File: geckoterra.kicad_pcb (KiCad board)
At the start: 2 copper layers, 50 x 50 mm, 24 parts, among them J1 AC_Output, J6 Conn_01x02, J7 Conn_01x02, J8 Conn_01x02, K1 SANYOU_SRD_Form_C, P1 AC_Input, Q1 2N3904, Q2 Q_NMOS_GDS, U1 PC817, U2 4N25

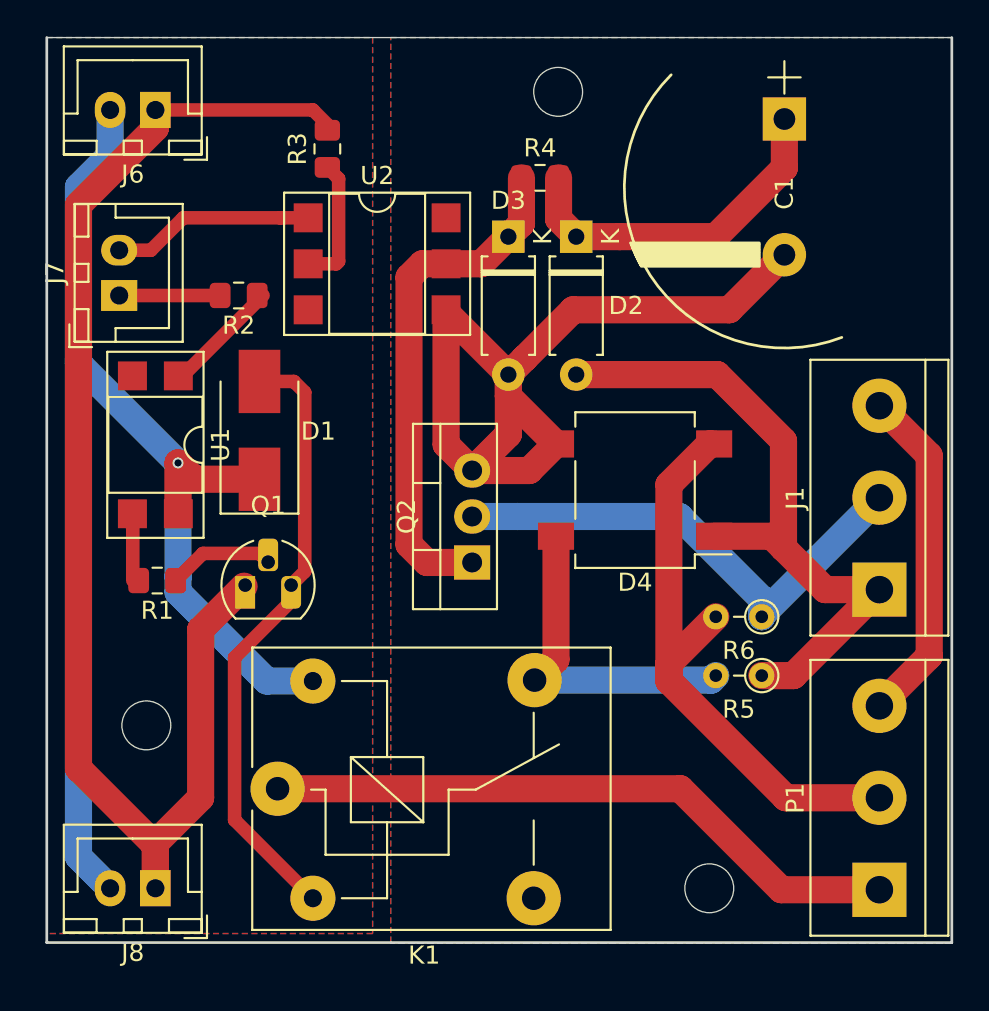
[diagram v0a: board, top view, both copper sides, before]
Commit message: Repair PCB considering footprints
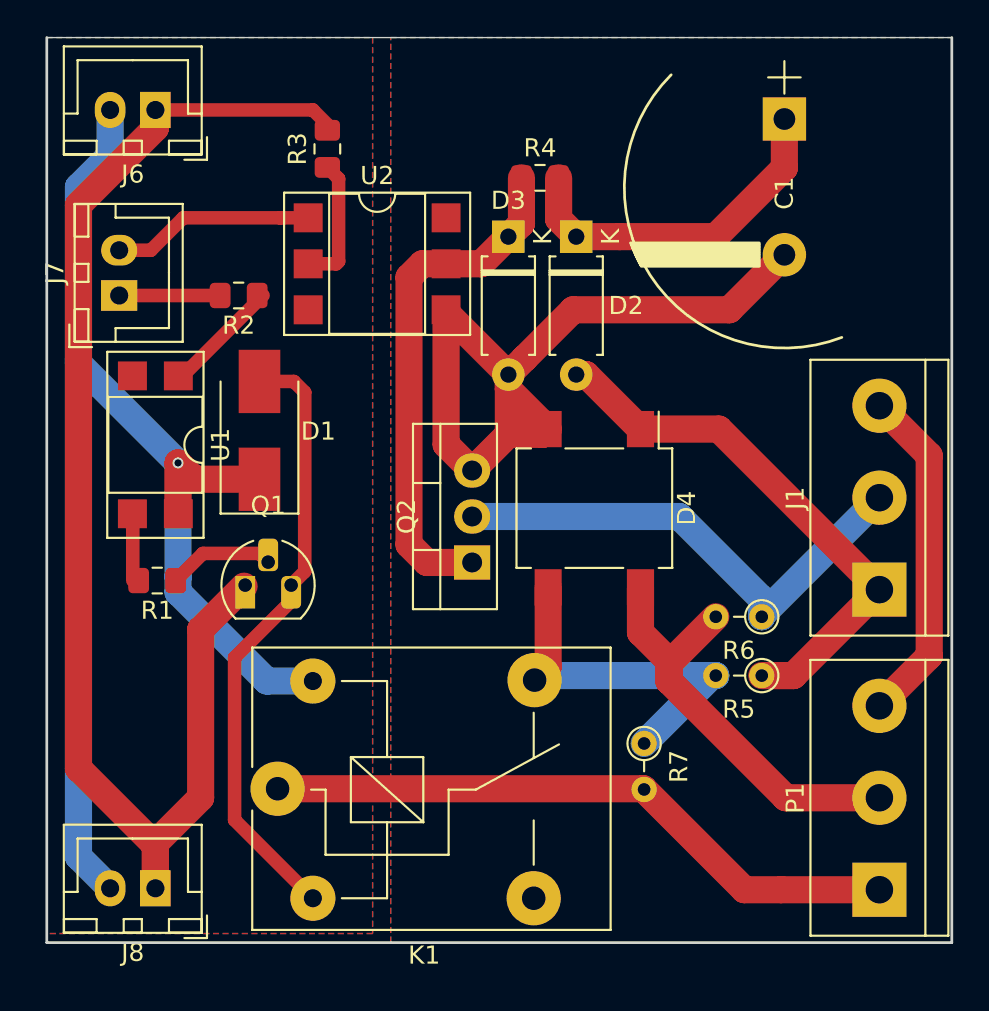
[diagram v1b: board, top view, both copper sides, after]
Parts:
- removed SC1 (x2), SC2: MountingHole_2.7mm_M2.5, Mounting_Holes:MountingHole_2.7mm_M2.5
- added R7: Shunt, Resistor_THT:R_Axial_DIN0204_L3.6mm_D1.6mm_P2.54mm_Vertical, F.Cu at (83.0, 89.0)
- moved D4 2.46 mm to (80.2, 76.0), turned to 270 degrees
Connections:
- D4 pad 2: Net-(D4-Pad2) -> Net-(C1-Pad2)
- D4 pad 3: Net-(C1-Pad2) -> Net-(D4-Pad3)
- K1 pad 4: Net-(D4-Pad4) -> Net-(D4-Pad3)
- P1 pad 2: Net-(D4-Pad2) -> Net-(D4-Pad4)
- R5 pad 2: Net-(D4-Pad4) -> Net-(D4-Pad3)
- R6 pad 2: Net-(D4-Pad2) -> Net-(D4-Pad4)
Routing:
- net Net-(D4-Pad2): track 33.2 -> 0.00 mm
- net Net-(D4-Pad3): track 0.00 -> 21.1 mm
- net Net-(D2-Pad2): track 39.3 -> 31.7 mm
- net Net-(D4-Pad4): track 18.5 -> 24.7 mm
- net Net-(C1-Pad2): track 48.8 -> 44.8 mm

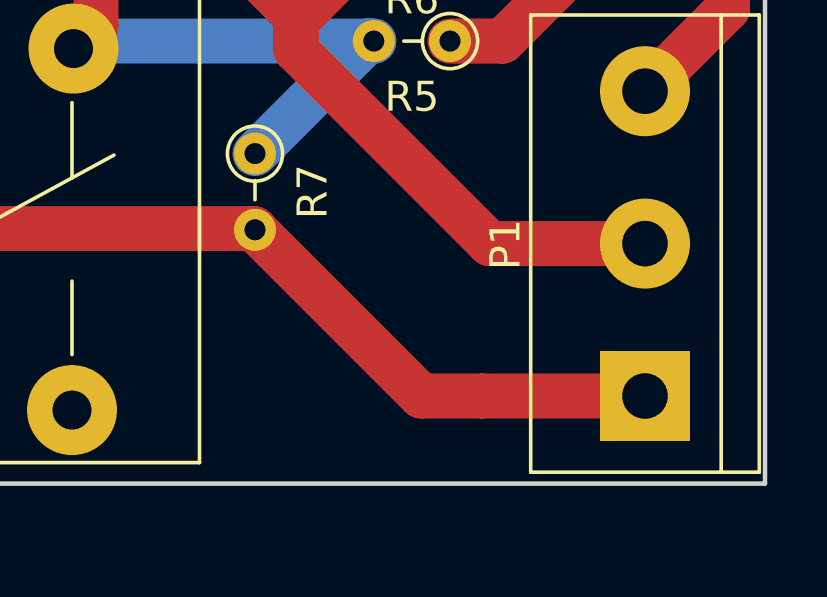
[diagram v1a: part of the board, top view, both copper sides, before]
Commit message: Add fuse
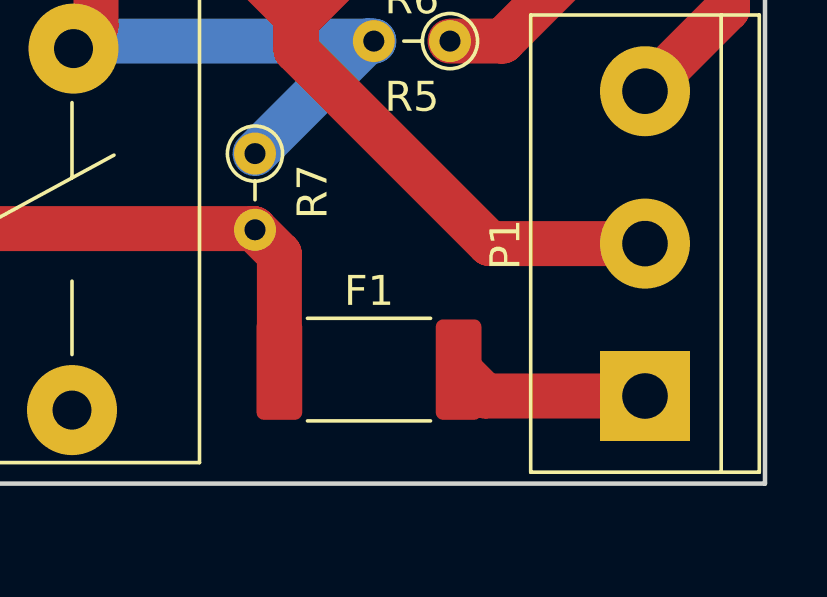
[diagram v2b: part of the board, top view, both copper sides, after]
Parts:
- added F1: Fuse, Fuse:Fuse_2512_6332Metric_Pad1.52x3.35mm_HandSolder, F.Cu at (86.8, 96.2)
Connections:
- K1 pad 1: Net-(K1-Pad1) -> Net-(F1-Pad1)
- P1 pad 1: Net-(K1-Pad1) -> Net-(F1-Pad2)
- R7 pad 2: Net-(K1-Pad1) -> Net-(F1-Pad1)
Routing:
- net Net-(K1-Pad1): track 35.6 -> 0.00 mm
- net Net-(F1-Pad1): track 0.00 -> 25.3 mm
- net Net-(F1-Pad2): track 0.00 -> 6.58 mm
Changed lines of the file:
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@@
     (thickness 1.6)
     (drawings 8)
-    (tracks 118)
+    (tracks 119)
     (zones 0)
-    (modules 22)
-    (nets 22)
+    (modules 23)
+    (nets 23)
   )
   (page A4)
@@
   (net 15 "Net-(R2-Pad1)")
   (net 16 "Net-(R3-Pad1)")
-  (net 17 "Net-(K1-Pad1)")
-  (net 18 "Net-(U2-Pad3)")
-  (net 19 "Net-(U2-Pad6)")
-  (net 20 "Net-(K1-Pad3)")
-  (net 21 "Net-(D4-Pad3)")
+  (net 17 "Net-(U2-Pad3)")
+  (net 18 "Net-(U2-Pad6)")
+  (net 19 "Net-(K1-Pad3)")
+  (net 20 "Net-(D4-Pad3)")
+  (net 21 "Net-(F1-Pad2)")
+  (net 22 "Net-(F1-Pad1)")
   (net_class Default "Ceci est la Netclass par défaut"
     (clearance 0.5)
@@
     (uvia_drill 0.1)
     (add_net "Net-(D4-Pad3)")
-    (add_net "Net-(K1-Pad1)")
+    (add_net "Net-(F1-Pad1)")
+    (add_net "Net-(F1-Pad2)")
     (add_net "Net-(K1-Pad3)")
     (add_net "Net-(U2-Pad3)")
@@
     (add_net "Net-(R3-Pad1)")
   )
+  (module Fuse:Fuse_2512_6332Metric_Pad1.52x3.35mm_HandSolder (layer F.Cu)
+    (at 86.8 96.2)
+    (descr "Fuse SMD 2512 (6332 Metric), square (rectangular) end terminal, IPC_7351 nominal with elongated pad for handsoldering. (Body size source: http://www.tortai-tech.com/upload/download/2011102023233369053.pdf), generated with kicad-footprint-generator")
+    (tags "resistor handsolder")
+    (attr smd)
+    (fp_text reference F1 (at 0 -2.62) (layer F.SilkS)
+      (effects (font (size 1 1) (thickness 0.15)))
+    )
+    (fp_text value Fuse (at 0 2.62) (layer F.Fab)
+      (effects (font (size 1 1) (thickness 0.15)))
+    )
+    (fp_line (start -3.15 1.6) (end -3.15 -1.6) (layer F.Fab) (width 0.1))
+    (fp_line (start -3.15 -1.6) (end 3.15 -1.6) (layer F.Fab) (width 0.1))
+    (fp_line (start 3.15 -1.6) (end 3.15 1.6) (layer F.Fab) (width 0.1))
+    (fp_line (start 3.15 1.6) (end -3.15 1.6) (layer F.Fab) (width 0.1))
+    (fp_line (start -2.052064 -1.71) (end 2.052064 -1.71) (layer F.SilkS) (width 0.12))
+    (fp_line (start -2.052064 1.71) (end 2.052064 1.71) (layer F.SilkS) (width 0.12))
+    (fp_line (start -4 1.92) (end -4 -1.92) (layer F.CrtYd) (width 0.05))
+    (fp_line (start -4 -1.92) (end 4 -1.92) (layer F.CrtYd) (width 0.05))
+    (fp_line (start 4 -1.92) (end 4 1.92) (layer F.CrtYd) (width 0.05))
+    (fp_line (start 4 1.92) (end -4 1.92) (layer F.CrtYd) (width 0.05))
+    (fp_text user %R (at 0 0) (layer F.Fab)
+      (effects (font (size 1 1) (thickness 0.15)))
+    )
+    (pad 1 smd roundrect (at -2.9875 0) (size 1.525 3.35) (layers F.Cu F.Paste F.Mask) (roundrect_rratio 0.163934)
+      (net 22 "Net-(F1-Pad1)"))
+    (pad 2 smd roundrect (at 2.9875 0) (size 1.525 3.35) (layers F.Cu F.Paste F.Mask) (roundrect_rratio 0.163934)
+      (net 21 "Net-(F1-Pad2)"))
+    (model ${KISYS3DMOD}/Fuse.3dshapes/Fuse_2512_6332Metric.wrl
+      (at (xyz 0 0 0))
+      (scale (xyz 1 1 1))
+      (rotate (xyz 0 0 0))
+    )
+  )
   (module Resistor_THT:R_Axial_DIN0204_L3.6mm_D1.6mm_P2.54mm_Vertical (layer F.Cu)
     (at 83 89 270)
@@
     )
     (pad 1 thru_hole circle (at 0 0 270) (size 1.4 1.4) (drill 0.7) (layers *.Cu *.Mask)
-      (net 21 "Net-(D4-Pad3)"))
+      (net 20 "Net-(D4-Pad3)"))
     (pad 2 thru_hole oval (at 2.54 0 270) (size 1.4 1.4) (drill 0.7) (layers *.Cu *.Mask)
-      (net 17 "Net-(K1-Pad1)"))
+      (net 22 "Net-(F1-Pad1)"))
     (model ${KISYS3DMOD}/Resistor_THT.3dshapes/R_Axial_DIN0204_L3.6mm_D1.6mm_P2.54mm_Vertical.wrl
       (at (xyz 0 0 0))
@@
       (net 2 "Net-(C1-Pad2)"))
     (pad 3 smd rect (at 4.37 2.55 270) (size 2 1.5) (layers F.Cu F.Paste F.Mask)
-      (net 21 "Net-(D4-Pad3)"))
+      (net 20 "Net-(D4-Pad3)"))
     (pad 4 smd rect (at 4.37 -2.55 270) (size 2 1.5) (layers F.Cu F.Paste F.Mask)
       (net 7 "Net-(D4-Pad4)"))
@@
     (fp_circle (center 0 0) (end 0.8 0) (layer F.Fab) (width 0.1))
     (pad 2 thru_hole oval (at 2.54 0 180) (size 1.4 1.4) (drill 0.7) (layers *.Cu *.Mask)
-      (net 21 "Net-(D4-Pad3)"))
+      (net 20 "Net-(D4-Pad3)"))
     (pad 1 thru_hole circle (at 0 0 180) (size 1.4 1.4) (drill 0.7) (layers *.Cu *.Mask)
       (net 5 "Net-(D2-Pad2)"))
@@
     (fp_arc (start 0 -3.87) (end -1 -3.87) (angle -180) (layer F.SilkS) (width 0.12))
     (pad 6 smd rect (at 3.81 -2.54) (size 1.6 1.6) (layers F.Cu F.Paste F.Mask)
-      (net 19 "Net-(U2-Pad6)"))
+      (net 18 "Net-(U2-Pad6)"))
     (pad 3 smd rect (at -3.81 2.54) (size 1.6 1.6) (layers F.Cu F.Paste F.Mask)
-      (net 18 "Net-(U2-Pad3)"))
+      (net 17 "Net-(U2-Pad3)"))
     (pad 5 smd rect (at 3.81 0) (size 1.6 1.6) (layers F.Cu F.Paste F.Mask)
       (net 6 "Net-(D3-Pad1)"))
@@
       (net 4 "Net-(D1-Pad2)"))
     (pad 3 thru_hole circle (at 14.15 6.05 90) (size 3 3) (drill 1.3) (layers *.Cu *.Mask)
-      (net 20 "Net-(K1-Pad3)"))
+      (net 19 "Net-(K1-Pad3)"))
     (pad 4 thru_hole circle (at 14.2 -6 90) (size 3 3) (drill 1.3) (layers *.Cu *.Mask)
-      (net 21 "Net-(D4-Pad3)"))
+      (net 20 "Net-(D4-Pad3)"))
     (pad 5 thru_hole circle (at 1.95 -5.95 90) (size 2.5 2.5) (drill 1) (layers *.Cu *.Mask)
       (net 3 +5V))
     (pad 1 thru_hole circle (at 0 0 90) (size 3 3) (drill 1.3) (layers *.Cu *.Mask)
-      (net 17 "Net-(K1-Pad1)"))
+      (net 22 "Net-(F1-Pad1)"))
     (model ${KISYS3DMOD}/Relay_THT.3dshapes/Relay_SPDT_SANYOU_SRD_Series_Form_C.wrl
       (at (xyz 0 0 0))
@@
     (fp_line (start 12.88 4) (end -2.72 4) (layer F.CrtYd) (width 0.05))
     (pad 1 thru_hole rect (at 0 0 90) (size 3 3) (drill 1.52) (layers *.Cu *.Mask)
-      (net 17 "Net-(K1-Pad1)"))
+      (net 21 "Net-(F1-Pad2)"))
     (pad 2 thru_hole circle (at 5.08 0 90) (size 3 3) (drill 1.52) (layers *.Cu *.Mask)
       (net 7 "Net-(D4-Pad4)"))
@@
   (segment (start 65.99 62.5) (end 66.123372 62.366628) (width 0.75) (layer F.Cu) (net 16))
   (segment (start 64.44 62.5) (end 65.99 62.5) (width 0.75) (layer F.Cu) (net 16))
-  (segment (start 90.58 97.08) (end 96 97.08) (width 1.5) (layer F.Cu) (net 17))
-  (segment (start 82.96 91.5) (end 83 91.54) (width 1.5) (layer F.Cu) (net 17))
-  (segment (start 62.75 91.5) (end 82.96 91.5) (width 1.5) (layer F.Cu) (net 17))
-  (segment (start 88.54 97.08) (end 83 91.54) (width 1.5) (layer F.Cu) (net 17))
-  (segment (start 90.58 97.08) (end 88.54 97.08) (width 1.5) (layer F.Cu) (net 17))
-  (segment (start 77.7 84.75) (end 76.95 85.5) (width 1.5) (layer F.Cu) (net 21))
-  (segment (start 77.7 80.37) (end 77.7 84.75) (width 1.5) (layer F.Cu) (net 21))
-  (segment (start 86.75 85.25) (end 83 89) (width 1.5) (layer B.Cu) (net 21))
-  (segment (start 86.96 85.25) (end 86.75 85.25) (width 1.5) (layer B.Cu) (net 21))
-  (segment (start 77.2 85.25) (end 76.95 85.5) (width 1.5) (layer B.Cu) (net 21))
-  (segment (start 86.96 85.25) (end 77.2 85.25) (width 1.5) (layer B.Cu) (net 21))
+  (segment (start 82.96 91.5) (end 83 91.54) (width 1.5) (layer F.Cu) (net 22))
+  (segment (start 62.75 91.5) (end 82.96 91.5) (width 1.5) (layer F.Cu) (net 22))
+  (segment (start 77.7 84.75) (end 76.95 85.5) (width 1.5) (layer F.Cu) (net 20))
+  (segment (start 77.7 80.37) (end 77.7 84.75) (width 1.5) (layer F.Cu) (net 20))
+  (segment (start 86.75 85.25) (end 83 89) (width 1.5) (layer B.Cu) (net 20))
+  (segment (start 86.96 85.25) (end 86.75 85.25) (width 1.5) (layer B.Cu) (net 20))
+  (segment (start 77.2 85.25) (end 76.95 85.5) (width 1.5) (layer B.Cu) (net 20))
+  (segment (start 86.96 85.25) (end 77.2 85.25) (width 1.5) (layer B.Cu) (net 20))
+  (segment (start 90.6675 97.08) (end 89.7875 96.2) (width 1.5) (layer F.Cu) (net 21))
+  (segment (start 96 97.08) (end 90.6675 97.08) (width 1.5) (layer F.Cu) (net 21))
+  (segment (start 83.8125 92.3525) (end 83 91.54) (width 1.5) (layer F.Cu) (net 22))
+  (segment (start 83.8125 96.2) (end 83.8125 92.3525) (width 1.5) (layer F.Cu) (net 22))
   (zone (net 10) (net_name GND) (layer F.Cu) (hatch edge 0.508)
     (connect_pads (clearance 0.508))
